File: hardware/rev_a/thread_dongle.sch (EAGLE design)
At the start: 5 parts, among them IC1 CP2102, J1 USB-A-MALE-PLUG

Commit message: added routed board and schematic
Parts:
- removed IC1: CP2102, silabs:CP2102
- added C1, C3, C5, C6: 0.1uF, passives:CAPACITOR0402_CAP
- added C2: 4.7uF, passives:CAPACITOR0402_CAP
- added C4, C7: 1.0uF, passives:CAPACITOR0402_CAP
- added C8, C9: 8pF, passives:CAPACITOR0402_CAP
- added D1: LED0603, leds:LED0603
- added J2: TC2030-JLINK-NL, connector:TC2030-JLINK-NL
- added R1: 10k, passives:RESISTOR0402_RES
- added R2, R3, R4, R5, R6, R7: 0, passives:RESISTOR0402_RES
- added R8: 1k, passives:RESISTOR0402_RES
- added U2: ESDR0502N, chips:ESDR0502N
- added U3: CP2102, silabs:CP2102
- added Y1: FH1600015, crystals:FH1600015
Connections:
- new net !RESET: J2.!RESET, R1.1, U1.!RESET, U3.!RST
- new net GND: B1.GND, C1.2, C2.2, C3.2, C4.2, C5.2, C6.2, C7.2, C8.2, C9.2, J1.GND, J2.GND, U1.GND, U1.GNDANA, U1.PA17, U2.GND, U3.GND, U3.GND@EXP, U3.GND@M
- new net N$1: B1.BAL_P, U1.RF_P
- new net N$10: C8.1, U1.XTAL2, Y1.2
- new net N$15: C5.1, U1.DVDD
- new net N$16: C6.1, U1.AVDD
- new net N$17: C7.1, U1.VDDCORE
- new net N$2: B1.BAL_N, U1.RF_N
- new net N$3: A1.ANTENNA, B1.ANT
- new net N$4: J1.D-, U2.D-, U3.D-
- new net N$5: J1.D+, U2.D+, U3.D+
- new net N$6: C3.1, C4.1, J1.+5V, U2.VUSB, U3.REGIN, U3.VBUS
- new net N$7: D1.CATHODE, R8.2
- new net N$8: R8.1, U1.PA27
- new net N$9: C9.1, U1.XTAL1, Y1.1
- new net SAM_CTS: R5.2, U3.RTS
- new net SAM_RTS: R4.2, U3.CTS
- new net SAM_RX: R3.2, R7.2, U3.TXD
- new net SAM_TX: R2.2, R6.2, U3.RXD
- new net SER1_P2_DBG_RX: U1.PA19
- new net SER1_P2_DBG_TX: U1.PA18
- new net SER2_P0: R6.1, U1.PA08
- new net SER2_P1: R7.1, U1.PA09
- new net SER2_P2: R2.1, R4.1, U1.PA14
- new net SER2_P3: R3.1, R5.1, U1.PA15
- new net SWCLK: J2.SWDCLK, U1.PA30
- new net SWDIO: J2.SWDIO, U1.PA31
- new net VCC: C1.1, C2.1, D1.ANODE, J2.VCC, R1.2, U1.VDDANA, U1.VDDIN, U1.VDDIO, U3.VDD
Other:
- note added: "OPENTHREAD DEFAULT CONFIGURATION"
- note added: "VALID FLOWCONTROL CONFIGURATION"
- moved on the sheet: A1, B1, J1, U1

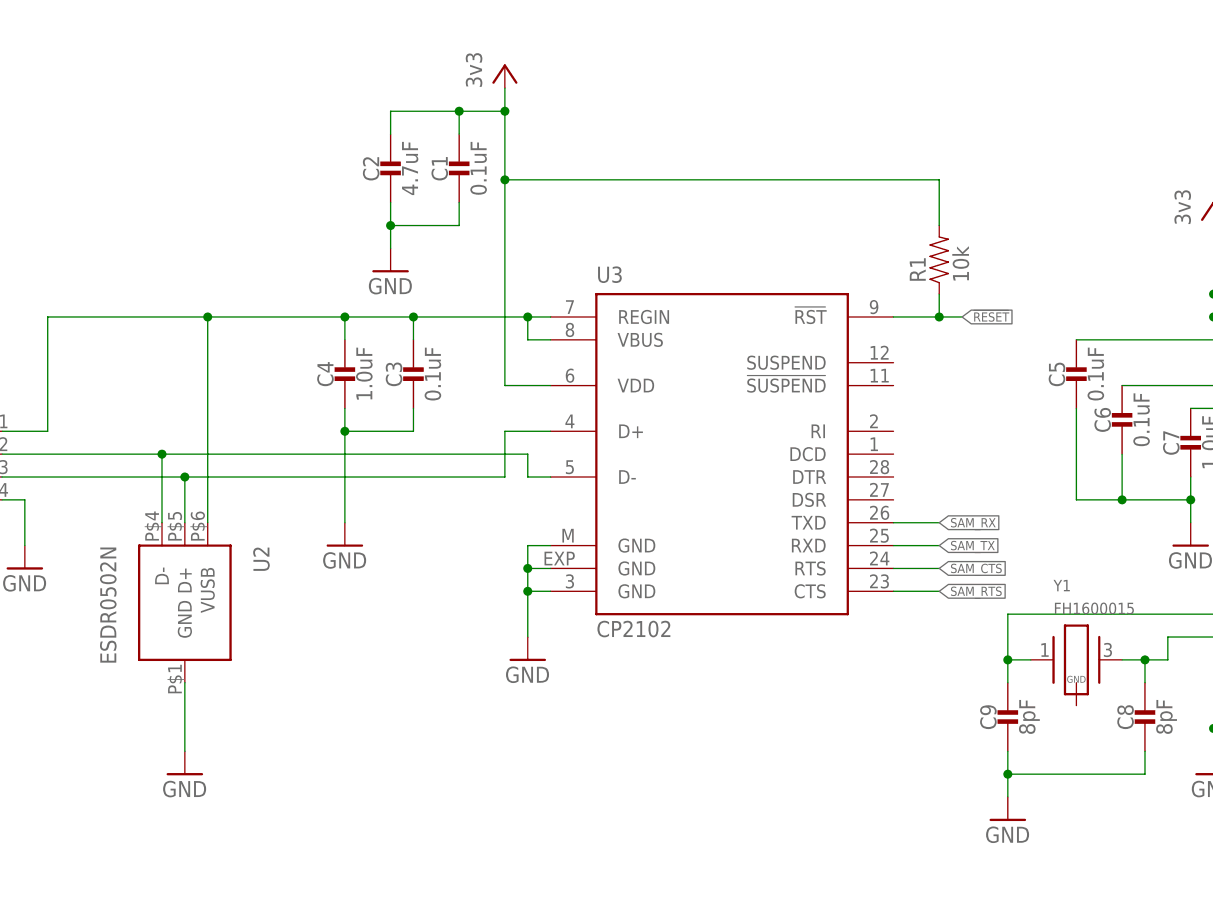
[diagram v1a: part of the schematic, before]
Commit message: smaller board, cheaper uart bridge
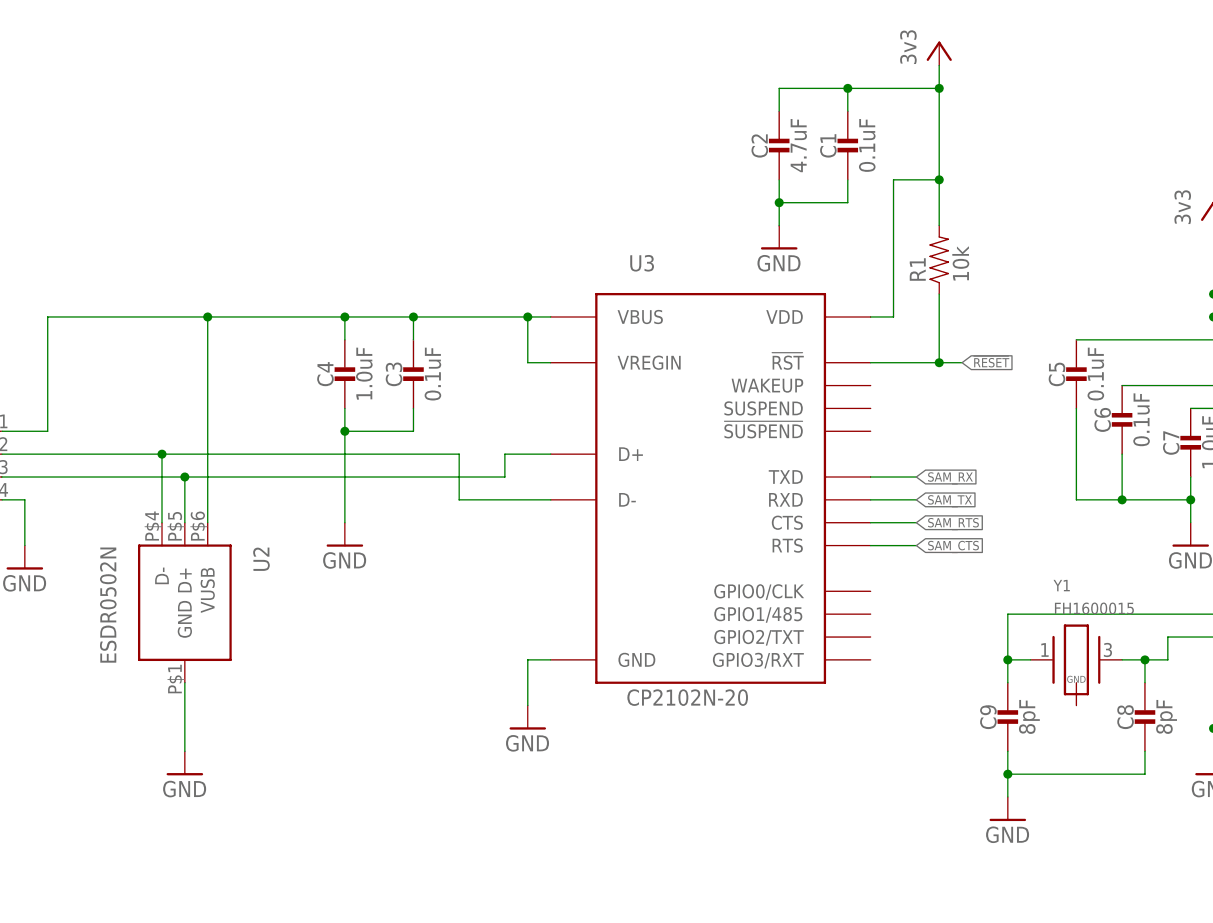
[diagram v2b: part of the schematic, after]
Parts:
- U3: value CP2102 -> CP2102N-20; device silabs:CP2102 -> chips:CP2102N-20
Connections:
- net GND: no longer U3.GND@EXP, U3.GND@M
- net N$6: now also U3.VREGIN; no longer U3.REGIN
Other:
- moved on the sheet: C1, C2

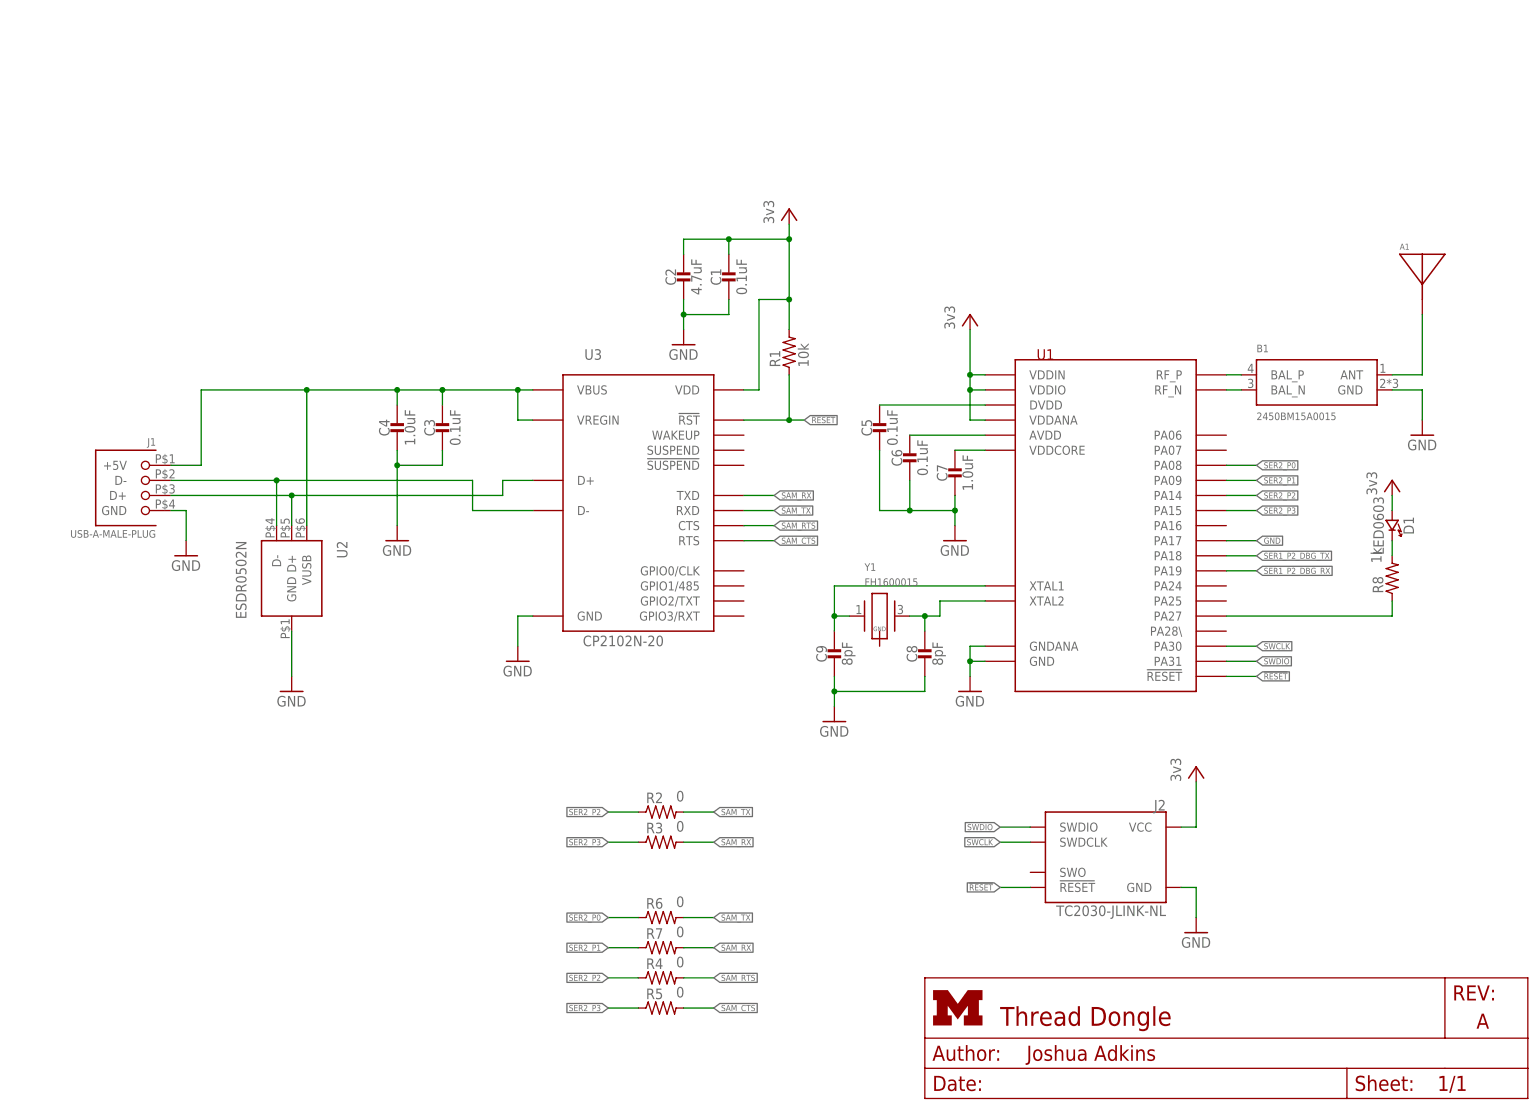
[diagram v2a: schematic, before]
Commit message: Update with KW21Z instead of SAMR21
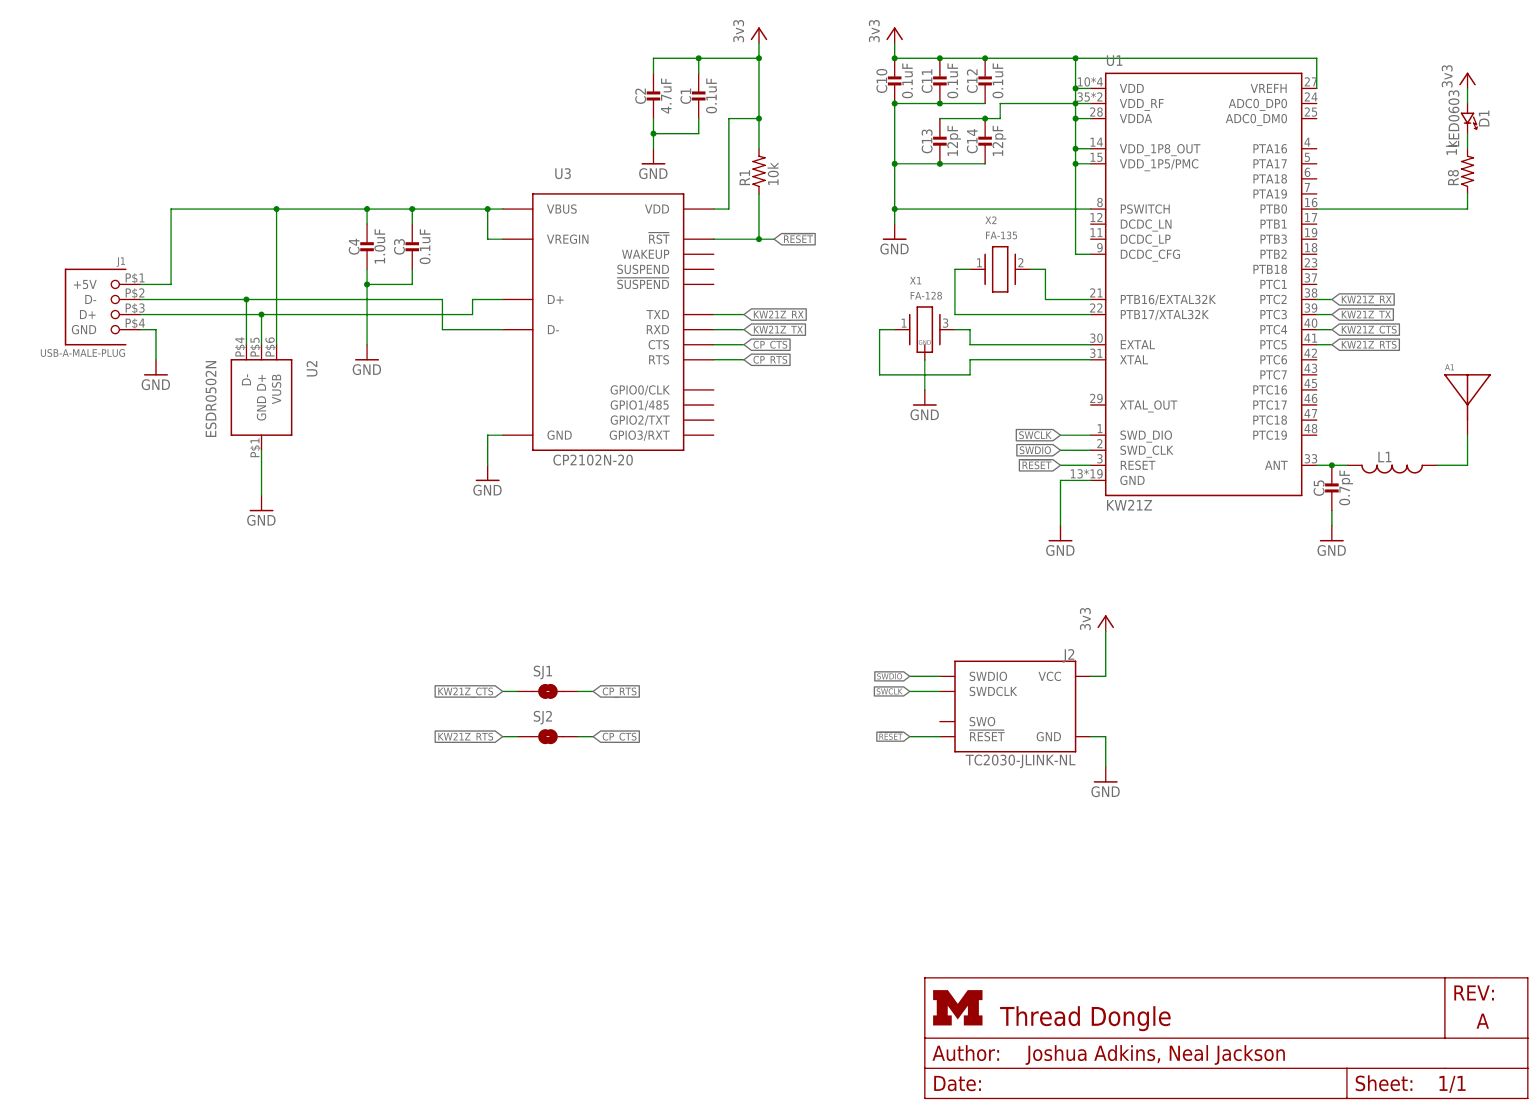
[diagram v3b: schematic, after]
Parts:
- removed B1: 2450BM15A0015, chips:2450BM15A0015
- removed C6: 0.1uF, passives:CAPACITOR0402_CAP
- removed C7: 1.0uF, passives:CAPACITOR0402_CAP
- removed C8, C9: 8pF, passives:CAPACITOR0402_CAP
- removed R2, R3, R4, R5, R6, R7: 0, passives:RESISTOR0402_RES
- removed Y1: FH1600015, crystals:FH1600015
- added C10, C11, C12: 0.1uF, passives:CAPACITOR0402_CAP
- added C13, C14: 12pF, passives:CAPACITOR0402_CAP
- added L1: (no value), passives:INDUCTOR0402
- added SJ1, SJ2: SOLDERJUMPERNC, headers:SOLDERJUMPERNC
- added X1: FA-128, crystals:FA-128
- added X2: FA-135, crystals:FA-135
- C5: value 0.1uF -> 0.7pF; DIGIKEY (none) -> 490-6267-1-ND
- U1: value (none) -> KW21Z; device chips:SAMR21E -> chips:KW21Z
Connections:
- net N$4 renamed D-
- net N$5 renamed D+
- net N$6 renamed 5V
- removed net N$1: B1.BAL_P, U1.RF_P
- removed net N$10: C8.1, U1.XTAL2, Y1.2
- removed net N$17: C7.1, U1.VDDCORE
- removed net N$2: B1.BAL_N, U1.RF_N
- removed net N$3: A1.ANTENNA, B1.ANT
- removed net N$9: C9.1, U1.XTAL1, Y1.1
- removed net SAM_CTS: R5.2, U3.RTS
- removed net SAM_RTS: R4.2, U3.CTS
- removed net SAM_RX: R3.2, R7.2, U3.TXD
- removed net SAM_TX: R2.2, R6.2, U3.RXD
- removed net SER1_P2_DBG_RX: U1.PA19
- removed net SER1_P2_DBG_TX: U1.PA18
- removed net SER2_P0: R6.1, U1.PA08
- removed net SER2_P1: R7.1, U1.PA09
- removed net SER2_P2: R2.1, R4.1, U1.PA14
- removed net SER2_P3: R3.1, R5.1, U1.PA15
- new net CP_CTS: SJ2.2, U3.CTS
- new net CP_RTS: SJ1.2, U3.RTS
- new net KW21Z_CTS: SJ1.1, U1.PTC4
- new net KW21Z_RTS: SJ2.1, U1.PTC5
- new net KW21Z_RX: U1.PTC2, U3.TXD
- new net KW21Z_TX: U1.PTC3, U3.RXD
- new net N$11: U1.EXTAL, X1.2
- new net N$12: U1.XTAL, X1.1
- new net N$13: C5.1, L1.2, U1.ANT
- new net N$14: U1.PTB17/XTAL32K, X2.1
- net !RESET: now also U1.RESET; no longer U1.!RESET
- net GND: now also C10.2, C11.2, C12.2, C13.2, C14.2, U1.PSWITCH, X1.GND; no longer B1.GND, C6.2, C7.2, C8.2, C9.2, U1.GNDANA, U1.PA17
- net N$15: now also U1.PTB16/EXTAL32K, X2.2; no longer C5.1, U1.DVDD
- net N$16: now also A1.ANTENNA, L1.1; no longer C6.1, U1.AVDD
- net N$8: now also U1.PTB0; no longer U1.PA27
- net SWCLK: now also U1.SWD_DIO; no longer U1.PA30
- net SWDIO: now also U1.SWD_CLK; no longer U1.PA31
- net VCC: now also C10.1, C11.1, C12.1, C13.1, C14.1, U1.DCDC_CFG, U1.VDD, U1.VDDA, U1.VDD_1P5/PMC, U1.VDD_1P8_OUT, U1.VDD_RF, U1.VREFH; no longer U1.VDDANA, U1.VDDIN, U1.VDDIO
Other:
- note added: "FLOWCONTROL ENABLE"
- note removed: "OPENTHREAD DEFAULT CONFIGURATION"
- note removed: "VALID FLOWCONTROL CONFIGURATION"
- moved on the sheet: A1, C1, C2, C3, C4, C5, D1, J1, J2, R1, R8, U2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
